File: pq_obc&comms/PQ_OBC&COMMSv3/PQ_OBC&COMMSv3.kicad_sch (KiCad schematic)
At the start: 66 parts, among them J1 Conn_01x10, J2 Conn_01x10, J3 Conn_01x10, J4 Conn_01x10, J6 U.FL-R-SMT-1_10_, U1 STM32L476RGTx, U2 SX1262IMLTRT, U3 BD2232G-GTR, U4 BD2232G-GTR, U5 RFswitch, U7 BD2232G-GTR, X1 12MHz, X2 FA-128_32.0000MF20X-K5, X3 32.768KHz

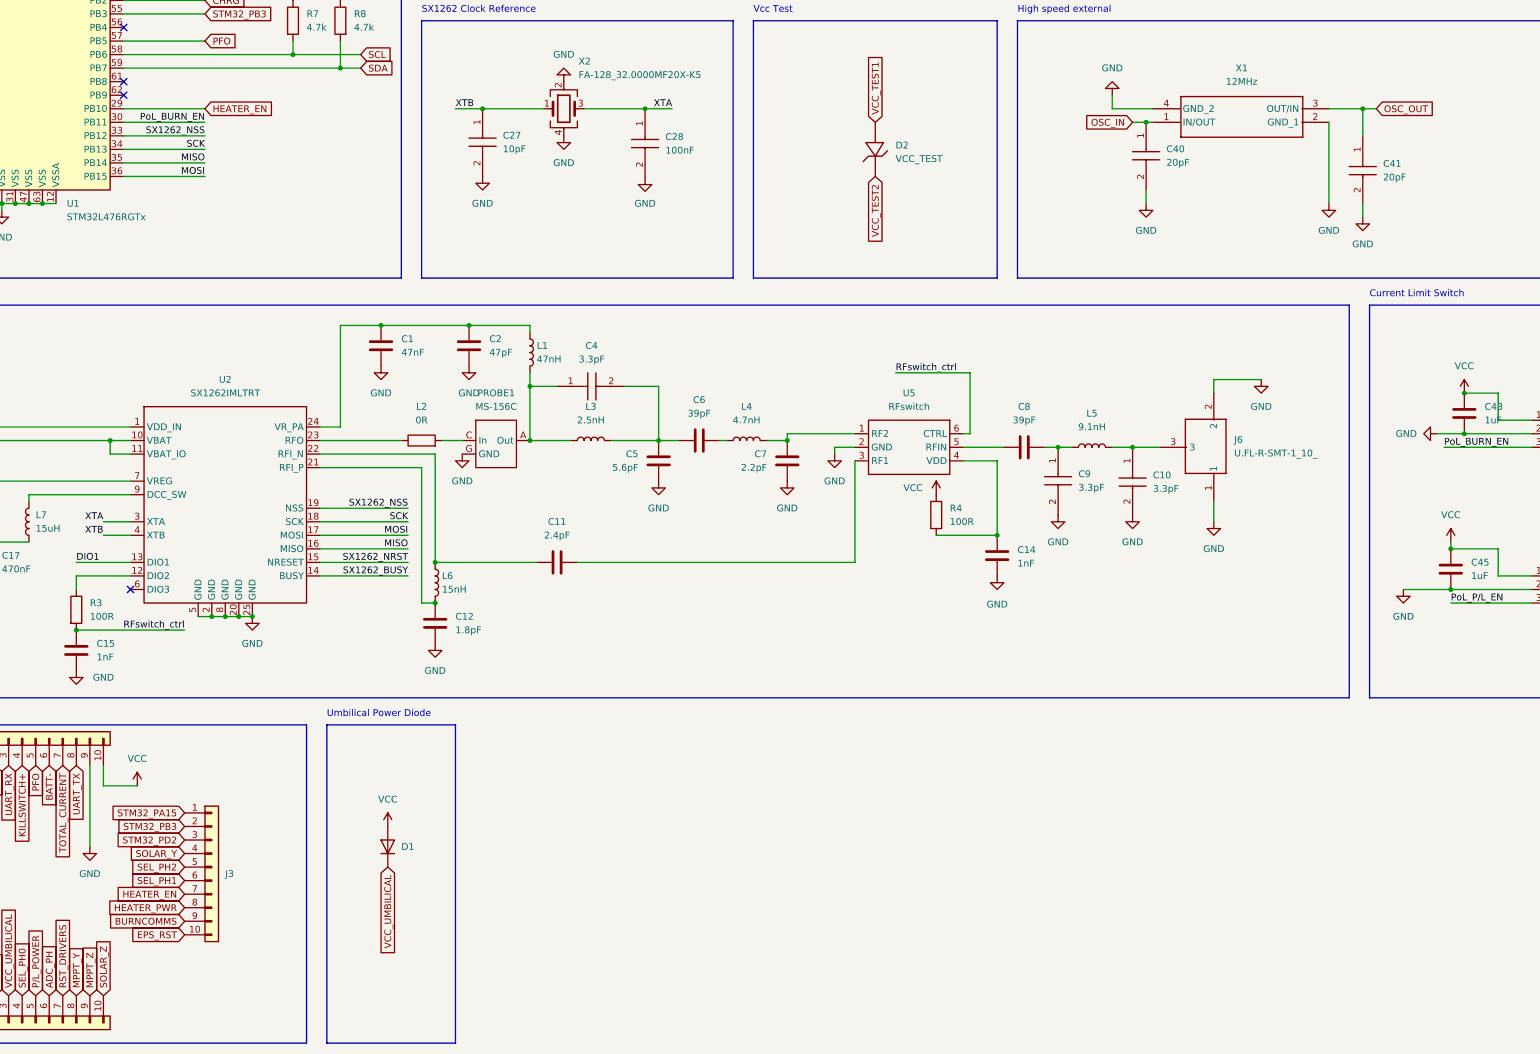
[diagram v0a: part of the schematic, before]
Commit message: gitkeep added to empty folders
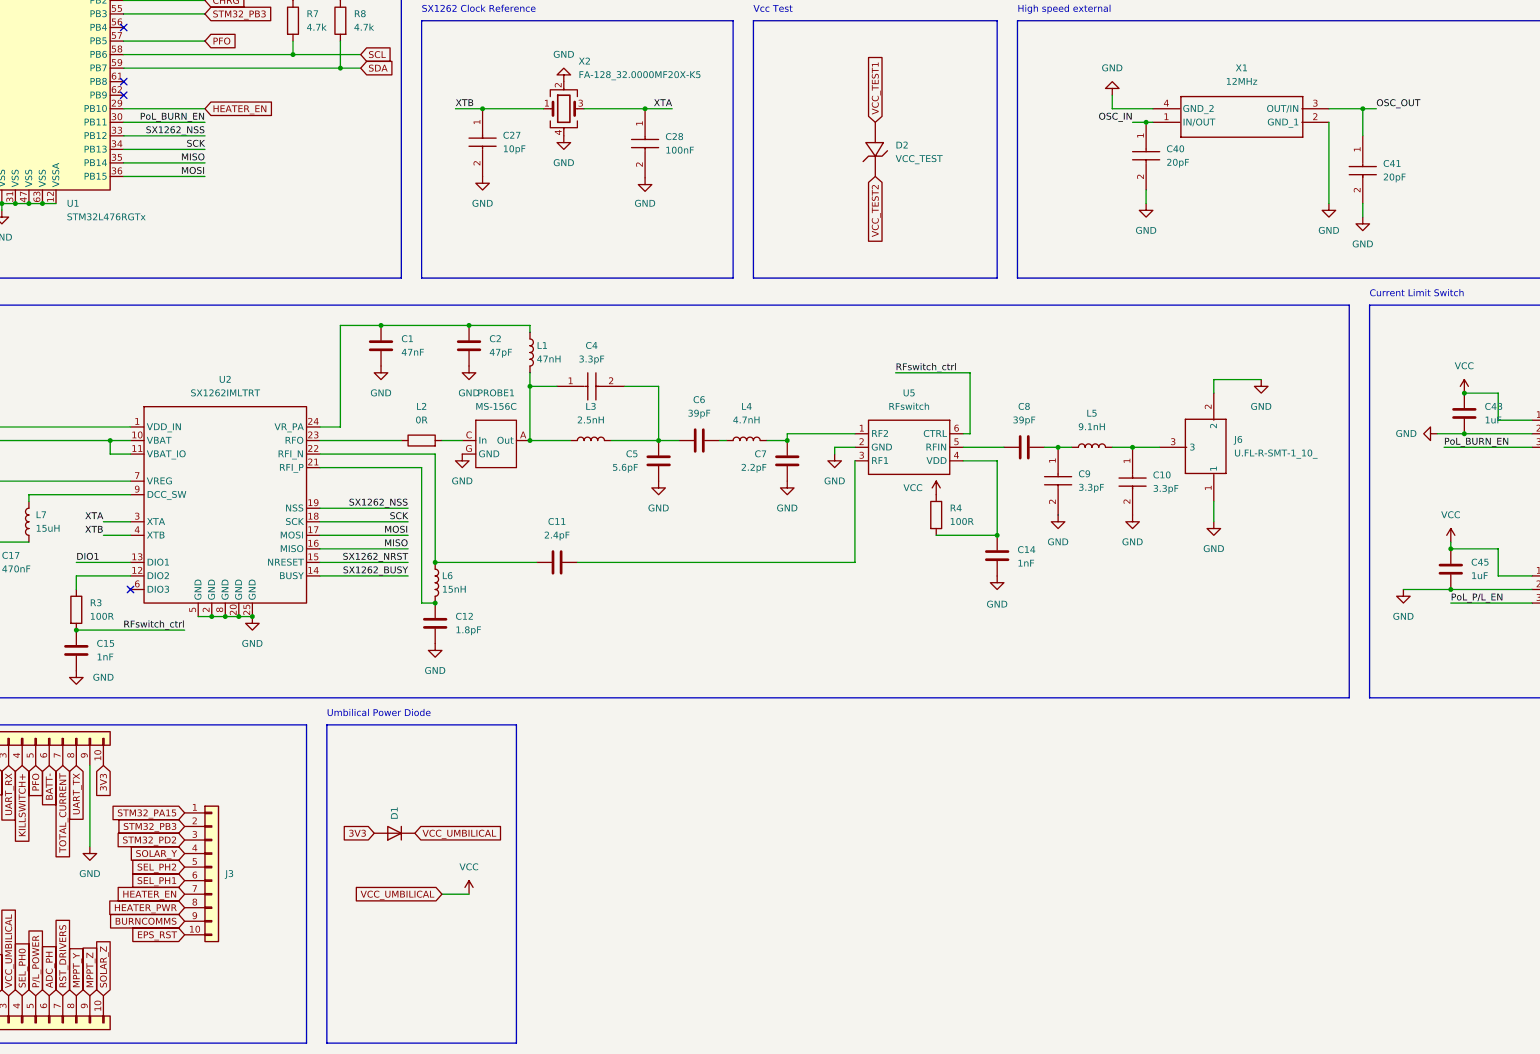
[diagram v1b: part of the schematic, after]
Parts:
- X1: footprint (none) -> GGS_Miscellaneous:ECX-32; CONTRIBUTOR danielCOMMS -> (none)
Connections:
- net VCC_UMBILICAL is gone; now on net VCC: D1.2 (K), J4.3 (Pin_3)
- net VCC: no longer D1.1 (A), J1.10 (Pin_10)
- new net 3V3: D1.1 (A), J1.10 (Pin_10)
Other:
- moved on the sheet: D1
